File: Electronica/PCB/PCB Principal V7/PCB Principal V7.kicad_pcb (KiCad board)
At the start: 2 copper layers, 151.8 x 90.5 mm, 23 parts, among them J1 Conexion Sensores, J10 Conn_01x01, J2 Power Monster, J3 On/Off General, J4 Power Input 2, J5 IDC Placa Botones, J6 Power Input 1, J7 Conn_01x01, J8 Conn_01x01, J9 Conn_01x01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

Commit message: pcb principal v7 sin terminar
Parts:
- removed J10, J7, J8, J9: Conn_01x01, Connector_PinHeader_2.54mm:PinHeader_1x01_P2.54mm_Vertical
- added ?: , , F.Cu at (226.4, 47.5)
- added J11: Conn_01x04_Pin, Connector_PinHeader_2.54mm:PinHeader_1x04_P2.54mm_Vertical, F.Cu at (81.2, 62.4)
- SW1: footprint Button_Switch_THT:SW_Slide_SPDT_Angled_CK_OS102011MA1Q -> Button_Switch_THT:SW_Slide_SPDT_Straight_CK_OS102011MS2Q
- moved D1 56.3 mm to (100.5, 60.5), turned to 0 degrees
- moved J6 48.0 mm to (111.1, 49.8), turned to 0 degrees
- moved D2 46.4 mm to (100.5, 65.5), turned to 0 degrees
- moved J5 40.9 mm to (210.3, 58.0), turned to 90 degrees
- moved D4 35.3 mm to (117.2, 114.7)
- moved J3 32.4 mm to (84.0, 114.7), turned to 90 degrees
- moved J4 23.3 mm to (91.8, 49.8), turned to 0 degrees
- moved R2 20.4 mm to (112.1, 110.8), turned to 0 degrees
- moved ? 18.6 mm to (224.6, 106.5)
- moved D3 16.9 mm to (213.0, 113.1)
- moved R1 16.9 mm to (209.6, 108.9)
- moved SW1 16.6 mm to (101.6, 114.6), turned to 180 degrees
- moved ? 13.8 mm to (81.2, 47.5)
- moved J2 13.2 mm to (84.0, 98.3)
- moved A2 12.9 mm to (132.6, 76.2)
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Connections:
- A1 pad 22: LED4 -> LED1
- U1 pad 6: LED1 -> LED4
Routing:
- net GND: track 444.3 -> 181.0 mm, vias 6 -> 0
- net VNano: track 216.1 -> 72.1 mm, vias 4 -> 0
- net +5V: track 223.8 -> 132.0 mm, vias 4 -> 0
- net ECHO 1: track 75.1 -> 0.00 mm, vias 4 -> 0
- net CNY 1: track 68.4 -> 0.00 mm
- net Net-(D1-K): track 13.5 -> 72.3 mm, vias 0 -> 4
- net CNY 2: track 57.9 -> 0.00 mm
- net BTN1: track 8.89 -> 65.0 mm
- net BTN2: track 8.89 -> 61.1 mm
- net PI+: track 25.4 -> 75.1 mm
- net LED2: track 48.9 -> 0.00 mm, vias 2 -> 0
- net ECHO 3: track 103.0 -> 63.6 mm, vias 2 -> 0
- net LED4: track 31.8 -> 0.00 mm, vias 2 -> 0
- net MOTORES: track 170.2 -> 201.1 mm
- net Net-(J2-Pin_2): track 24.7 -> 49.0 mm
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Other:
- board size 151.8 x 90.5 mm -> 151.8 x 74 mm

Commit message: PCB sensores v2 y principal v7 terminadas
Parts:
- removed the ? at (226.4, 47.5)
- Housing Botones: renamed from J5
- Housing Sensores: renamed from J1
- XT60 1: renamed from J4
- XT60 2: renamed from J6
- moved R1 109.7 mm to (99.9, 111.3)
- moved D3 108.1 mm to (105.0, 115.2)
- moved ? 12.4 mm to (230.0, 117.7)
- moved SW1 9.52 mm to (92.1, 115.5), turned to 0 degrees
- moved D1 5.46 mm to (95.4, 58.6)
- moved D2 5.46 mm to (95.4, 63.6)
- moved 74HC595 4.97 mm to (194.5, 68.3)
- moved D4 4.15 mm to (121.3, 115.2)
- moved R2 4.15 mm to (116.2, 111.3)
- moved Housing Sensores 2.93 mm to (185.6, 57.5)
- moved A2 2.91 mm to (129.7, 76.1)
- moved Housing Botones 2.89 mm to (208.2, 60.0)
- moved A1 2.16 mm to (186.4, 78.5)
- moved ? 0.83 mm to (80.8, 46.8)
- moved LM1 0.82 mm to (104.2, 82.5)
- renumbered U1 to 74HC595, J11 to TP
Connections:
- 74HC595 pad 4: LED2 -> TRIG 4
- 74HC595 pad 5: TRIG 4 -> TRIG 1
- 74HC595 pad 7: TRIG 1 -> LED2
- A1 pad 25: CNY 1 -> CNY 2
- A1 pad 26: CNY 2 -> CNY 1
- Housing Sensores pad 1: TRIG 2 -> ECHO 1
- Housing Sensores pad 10: TRIG 4 -> TRIG 1
- Housing Sensores pad 12: ECHO 1 -> unconnected-(J1-Pin_12-Pad12)
- Housing Sensores pad 13: CNY 3 -> CNY 1
- Housing Sensores pad 14: TRIG 1 -> unconnected-(J1-Pin_14-Pad14)
- Housing Sensores pad 2: ECHO 3 -> TRIG 2
- Housing Sensores pad 5: TRIG 5 -> ECHO 3
- Housing Sensores pad 6: unconnected-(J1-Pin_6-Pad6) -> TRIG 5
- Housing Sensores pad 7: ECHO 5 -> ECHO 4
- Housing Sensores pad 8: ECHO 4 -> TRIG 4
- Housing Sensores pad 9: CNY 1 -> ECHO 5
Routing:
- net +5V: track 132.0 -> 307.3 mm, vias 0 -> 4
- net GND: track 181.0 -> 344.9 mm, vias 0 -> 4
- net VNano: track 72.1 -> 222.9 mm, vias 0 -> 4
- net ECHO 4: track 0.00 -> 138.9 mm
- net ECHO 5: track 0.00 -> 127.0 mm
- net MOTORES: track 201.1 -> 83.6 mm
- net CNY 2: track 0.00 -> 107.9 mm, vias 0 -> 2
- net CNY 1: track 0.00 -> 95.8 mm, vias 0 -> 2
- net ECHO 1: track 0.00 -> 91.7 mm
- net LED3: track 0.00 -> 67.6 mm, vias 0 -> 2
- net ECHO 3: track 63.6 -> 113.4 mm
- net LED4: track 0.00 -> 47.3 mm, vias 0 -> 2
- net BTN2: track 61.1 -> 43.0 mm
- net BTN1: track 65.0 -> 47.5 mm
- net LED1: track 68.9 -> 52.1 mm
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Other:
- board size 151.8 x 74 mm -> 155.5 x 77.2 mm
- board text added: "CDR 2024"
- board text added: "Chicken Little V7"

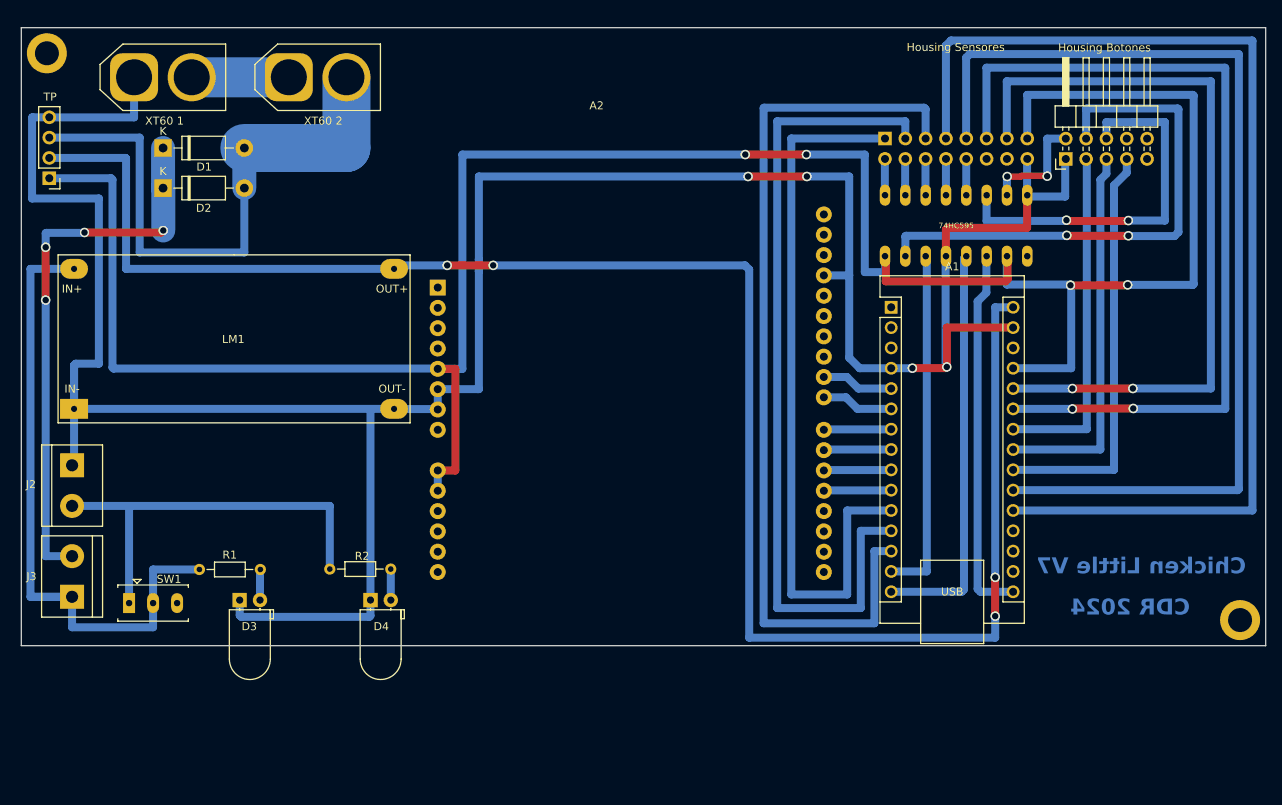
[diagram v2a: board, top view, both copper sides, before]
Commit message: placas
Seligrafis y capa inferior de:
Botones v2
Sensores v2
Principal v7

Co-Authored-By: EituCher18 <112017792+EituCher18@users.noreply.github.com>
Co-Authored-By: Aiden Maid Perez <60515813+Aid-Code@users.noreply.github.com>
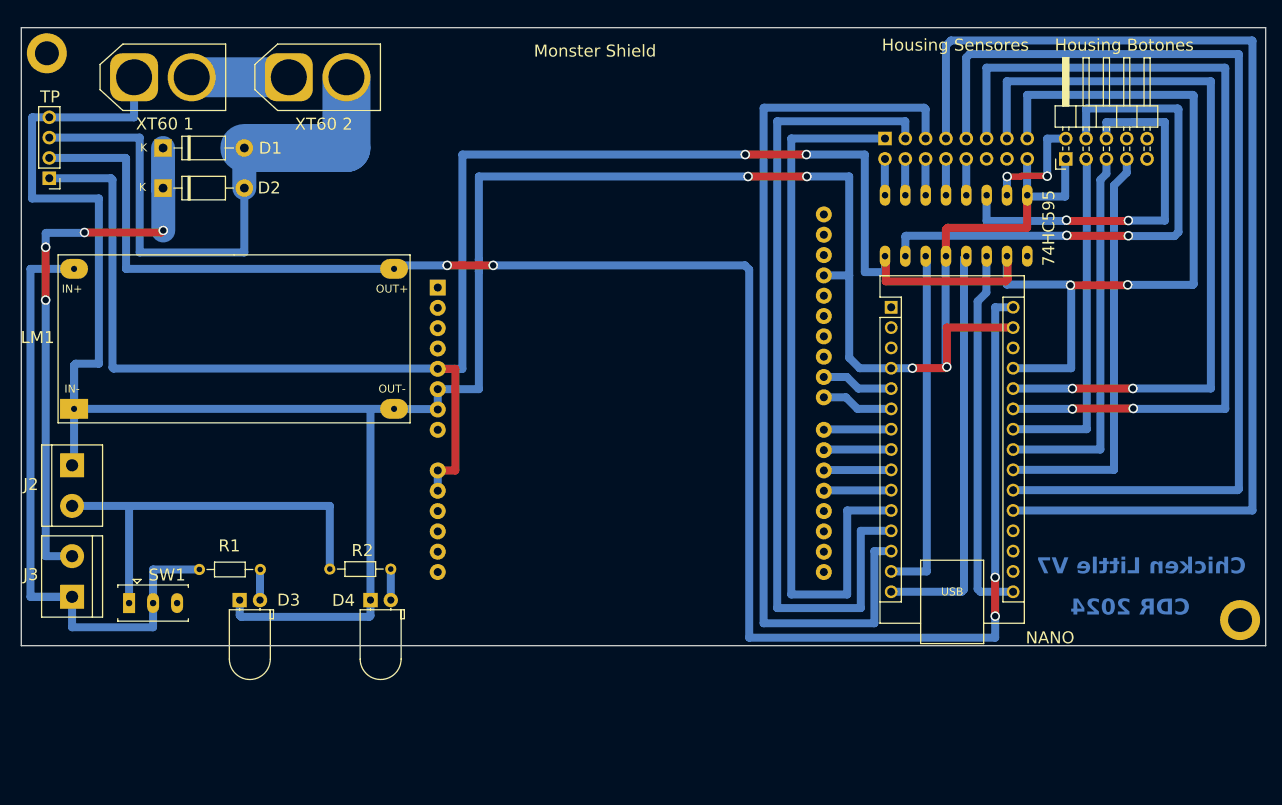
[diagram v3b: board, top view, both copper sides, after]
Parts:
- Monster Shield: renamed from A2
- renumbered A1 to NANO
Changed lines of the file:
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@@
 		(tags "switch SPDT")
 		(property "Reference" "SW1"
-			(at 3.99 -2.99 360)
+			(at 3.755 -3.515 0)
 			(layer "F.SilkS")
 			(effects
 				(font
-					(size 1 1)
+					(size 1.5 1.5)
 					(thickness 0.15)
 				)
@@
 		)
 		(property "Value" "On/Off Motores"
-			(at 2 3 360)
+			(at 2 3 0)
 			(layer "F.Fab")
 			(effects
@@
 		)
 		(fp_text user "${REFERENCE}"
-			(at 3.99 -2.99 360)
+			(at 3.99 -2.99 0)
 			(layer "F.Fab")
 			(effects
@@
 		(tags "Through hole angled pin header THT 2x05 2.54mm double row")
 		(property "Reference" "Housing Botones"
-			(at 13.91 4.835 0)
+			(at 14.23 7.305 0)
 			(layer "F.SilkS")
 			(effects
 				(font
-					(size 1 1)
+					(size 1.5 1.5)
 					(thickness 0.15)
 				)
@@
 		(tags "LED diameter 5.0mm z-position of LED center 3.0mm 2 pins")
 		(property "Reference" "D4"
-			(at 1.35 3.3 0)
+			(at -3.37 0.03 0)
 			(layer "F.SilkS")
 			(effects
 				(font
-					(size 1 1)
+					(size 1.5 1.5)
 					(thickness 0.15)
 				)
@@
 		(tags "XT60 female vertical")
 		(property "Reference" "XT60 1"
-			(at 3.8 5.45 180)
+			(at 3.84 5.83 0)
 			(layer "F.SilkS")
 			(effects
 				(font
-					(size 1 1)
+					(size 1.5 1.5)
 					(thickness 0.15)
 				)
@@
 		(tags "XT60 female vertical")
 		(property "Reference" "XT60 2"
-			(at 4.304 5.45 180)
+			(at 4.364 5.86 180)
 			(layer "F.SilkS")
 			(effects
 				(font
-					(size 1 1)
+					(size 1.5 1.5)
 					(thickness 0.15)
 				)
@@
 		(tags "terminal block bornier2")
 		(property "Reference" "J3"
-			(at 2.54 -5.08 0)
+			(at 2.78 -5.16 180)
 			(layer "F.SilkS")
 			(effects
 				(font
-					(size 1 1)
+					(size 1.5 1.5)
 					(thickness 0.15)
 				)
@@
 		(tags "Resistor Axial_DIN0204 series Axial Horizontal pin pitch 7.62mm 0.167W length 3.6mm diameter 1.6mm")
 		(property "Reference" "R2"
-			(at 4.035 -1.625 0)
+			(at 4.075 -2.325 0)
 			(layer "F.SilkS")
 			(effects
 				(font
-					(size 1 1)
+					(size 1.5 1.5)
 					(thickness 0.15)
 				)
@@
 		(tags "Resistor Axial_DIN0204 series Axial Horizontal pin pitch 7.62mm 0.167W length 3.6mm diameter 1.6mm")
 		(property "Reference" "R1"
-			(at 3.79 -1.825 0)
+			(at 3.745 -2.955 0)
 			(layer "F.SilkS")
 			(effects
 				(font
-					(size 1 1)
+					(size 1.5 1.5)
 					(thickness 0.15)
 				)
@@
 			(effects
 				(font
-					(size 1 1)
+					(size 1.5 1.5)
 					(thickness 0.15)
 				)
@@
 		(tags "LED diameter 5.0mm z-position of LED center 3.0mm 2 pins")
 		(property "Reference" "D3"
-			(at 1.2 3.3 0)
+			(at 6.12 0 0)
 			(layer "F.SilkS")
 			(effects
 				(font
-					(size 1 1)
+					(size 1.5 1.5)
 					(thickness 0.15)
 				)
@@
 		(tags "Diode DO-41_SOD81 series Axial Horizontal pin pitch 10.16mm  length 5.2mm diameter 2.7mm")
 		(property "Reference" "D1"
-			(at 5.13 2.36 0)
+			(at 13.41 0.02 0)
 			(layer "F.SilkS")
 			(effects
 				(font
-					(size 1 1)
+					(size 1.5 1.5)
 					(thickness 0.15)
 				)
@@
 		)
 		(fp_text user "K"
-			(at 0 -2.1 0)
+			(at -2.42 -0.04 0)
 			(layer "F.SilkS")
 			(effects
@@
 		(descr "Arduino Nano, http://www.mouser.com/pdfdocs/Gravitech_Arduino_Nano3_0.pdf")
 		(tags "Arduino Nano")
-		(property "Reference" "A1"
-			(at 7.62 -5.08 0)
+		(property "Reference" "NANO"
+			(at 19.86 41.31 0)
 			(layer "F.SilkS")
 			(effects
 				(font
-					(size 1 1)
+					(size 1.5 1.5)
 					(thickness 0.15)
 				)
@@
 		(tags "terminal block bornier2")
 		(property "Reference" "J2"
-			(at 2.4 5.15 180)
+			(at 2.4 5.15 0)
 			(layer "F.SilkS")
 			(effects
 				(font
-					(size 1 1)
+					(size 1.5 1.5)
 					(thickness 0.15)
 				)
@@
 		(at 104.25 82.5 90)
 		(property "Reference" "LM1"
-			(at -0.05 -0.1 0)
+			(at 0.17 -24.56 0)
 			(layer "F.SilkS")
 			(effects
 				(font
-					(size 1 1)
+					(size 1.5 1.5)
 					(thickness 0.15)
 				)
@@
 		(tags "Diode DO-41_SOD81 series Axial Horizontal pin pitch 10.16mm  length 5.2mm diameter 2.7mm")
 		(property "Reference" "D2"
-			(at 5.08 2.5 0)
+			(at 13.26 -0.02 0)
 			(layer "F.SilkS")
 			(effects
 				(font
-					(size 1 1)
+					(size 1.5 1.5)
 					(thickness 0.15)
 				)
@@
 		)
 		(fp_text user "K"
-			(at 0 -2.1 0)
+			(at -2.57 -0.11 0)
 			(layer "F.SilkS")
 			(effects
@@
 		(tags "Through hole angled pin header THT 2x08 2.54mm double row")
 		(property "Reference" "Housing Sensores"
-			(at -11.41 -8.835 180)
+			(at -11.68 -8.795 180)
 			(layer "F.SilkS")
 			(effects
 				(font
-					(size 1 1)
+					(size 1.5 1.5)
 					(thickness 0.15)
 				)
@@
 		(descr "<b>Dual In Line Package</b>")
 		(property "Reference" "74HC595"
-			(at 0 0 0)
+			(at 11.57 0.29 90)
 			(layer "F.SilkS")
 			(effects
 				(font
-					(size 0.70009 0.70009)
+					(size 1.5 1.5)
 					(thickness 0.15)
 				)
@@
 		(descr "Arduino UNO R3, http://www.mouser.com/pdfdocs/Gravitech_Arduino_Nano3_0.pdf")
 		(tags "Arduino UNO R3")
-		(property "Reference" "A2"
-			(at -22.743 -19.854 180)
+		(property "Reference" "Monster Shield"
+			(at -29.565 -19.66 180)
 			(layer "F.SilkS")
 			(effects
 				(font
-					(size 1 1)
+					(size 1.5 1.5)
 					(thickness 0.15)
 				)
